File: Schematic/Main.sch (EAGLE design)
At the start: 83 parts, among them IC1 PIC18F4550_40, IC2 7805, IC4 AD7734, IC5 AD780, IC7 7805, K1 SRD-24VDC-SL-C, K2 SRD-24VDC-SL-C, Q1 20MHz, Q2 3.579545MHz, T1 2N2222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

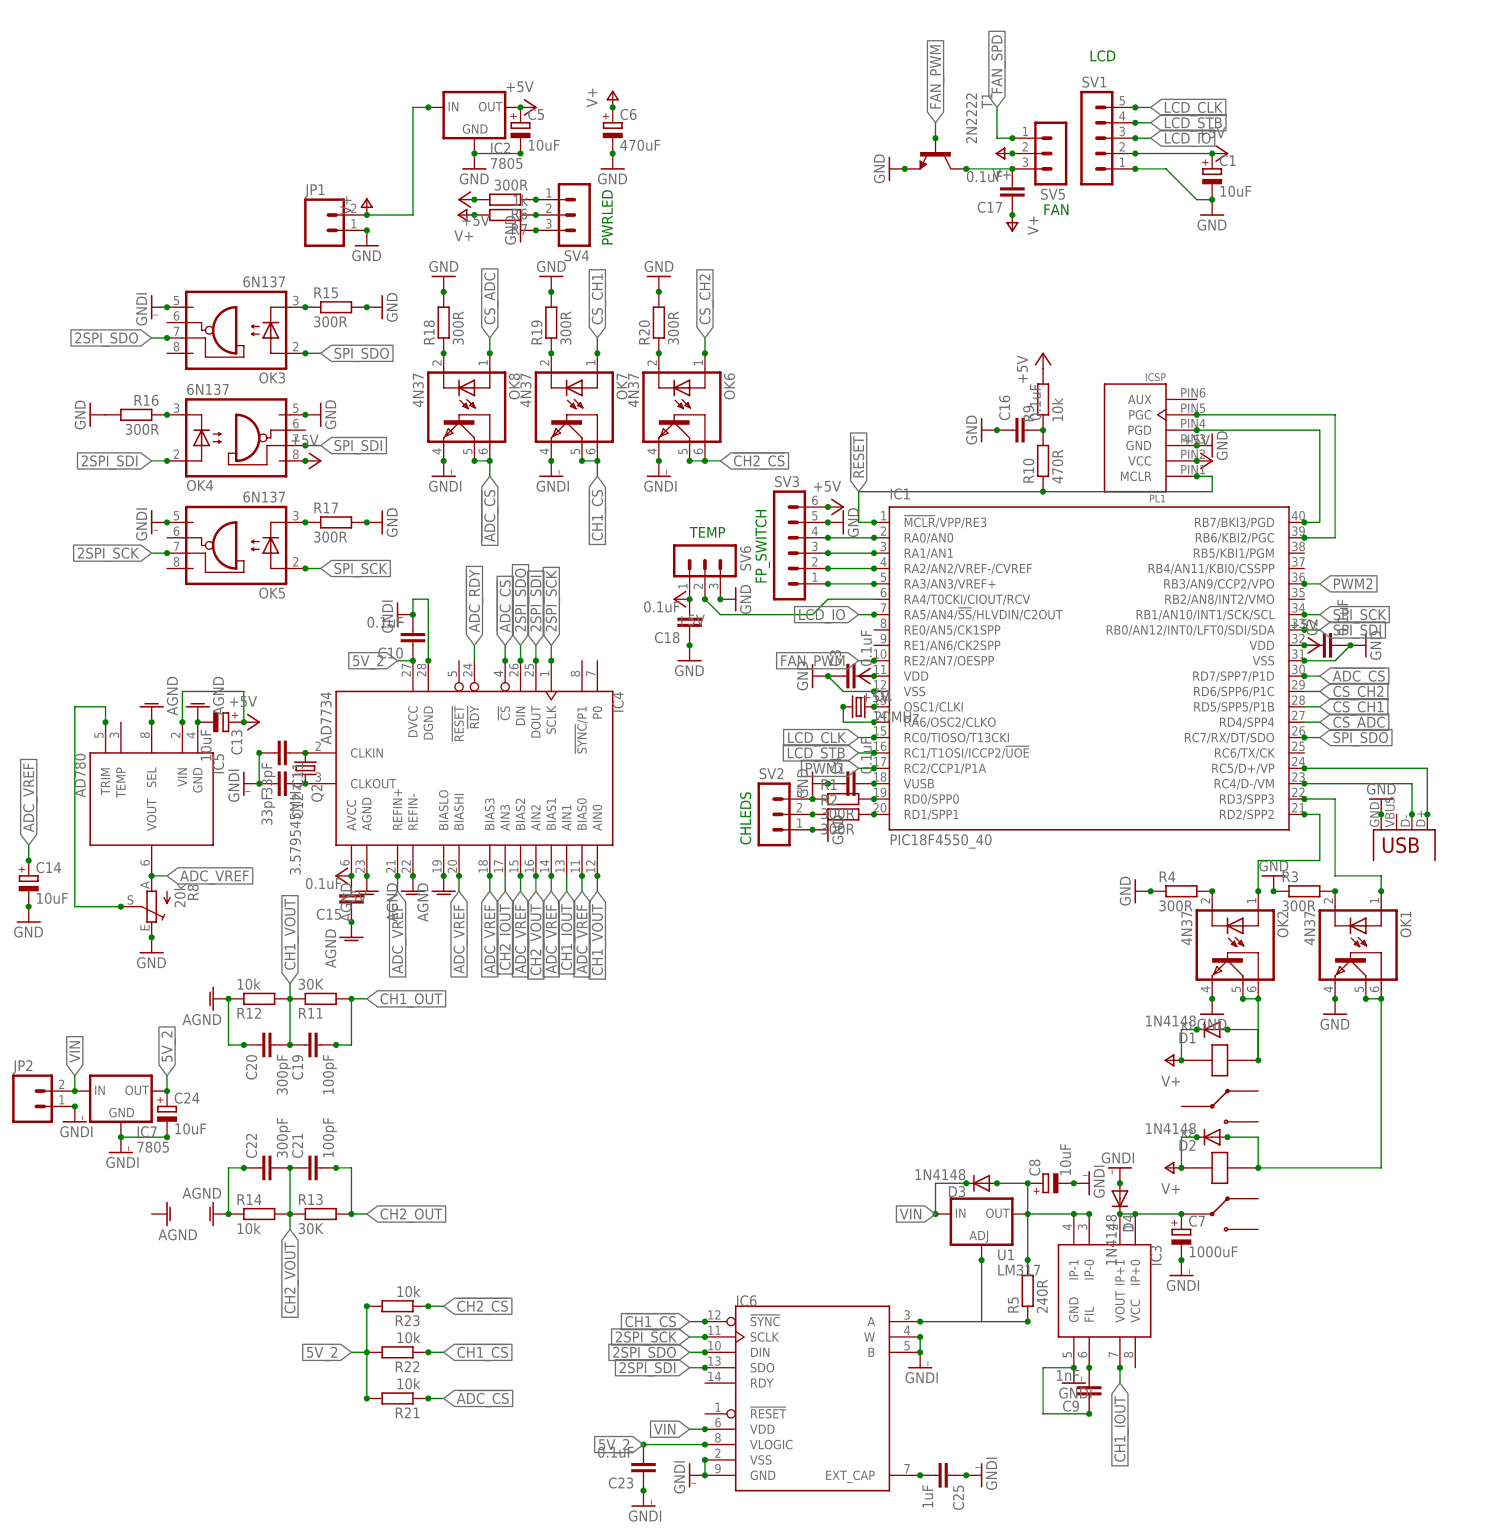
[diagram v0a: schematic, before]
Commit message: Got rid of the metric crapton of isolation as it wasn't really needed.
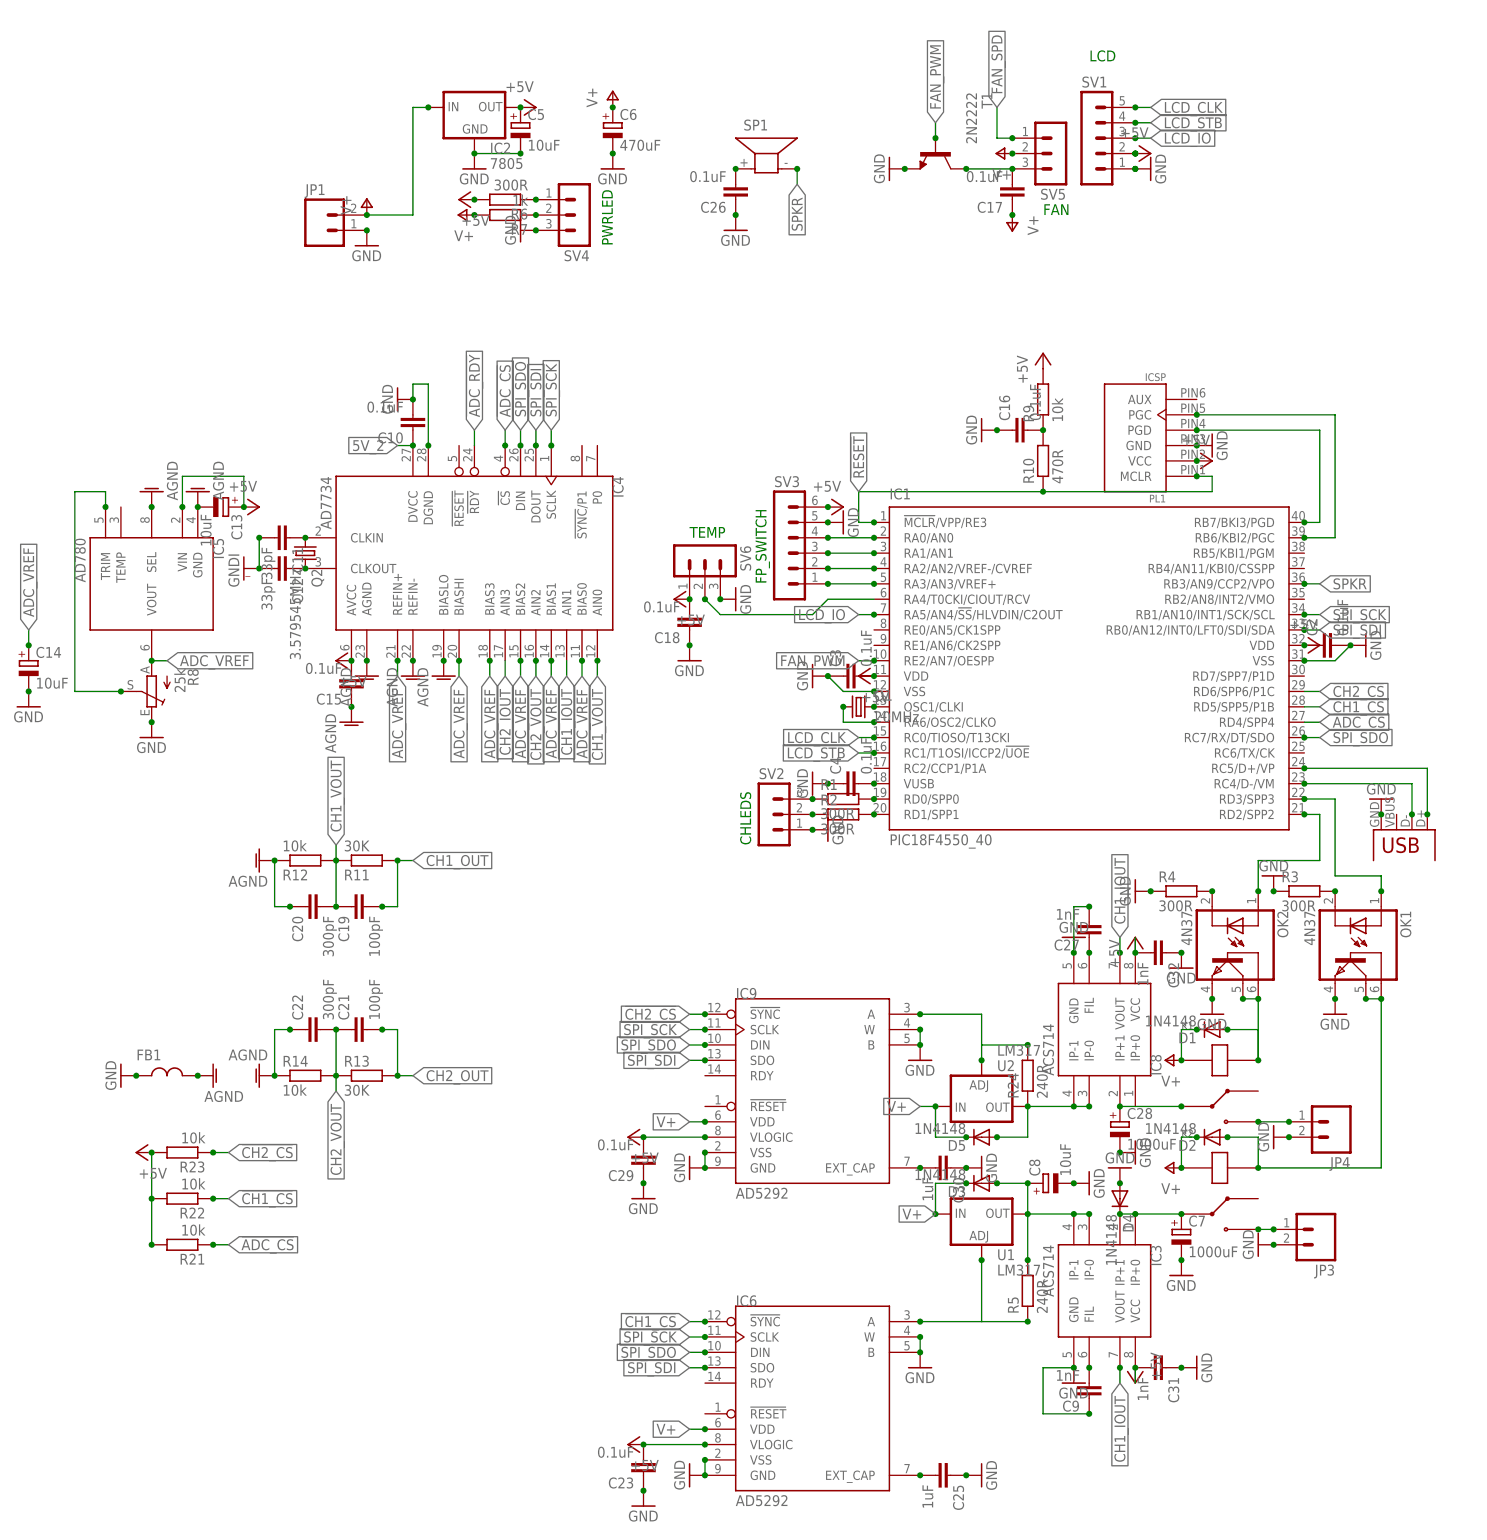
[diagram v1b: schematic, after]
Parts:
- removed C1, C24: 10uF, rcl:CPOL-EUE2.5-5
- removed IC7: 7805, v-reg:78MXXS
- removed JP2: (no value), SparkFun:M023.5MM
- removed OK3, OK4, OK5: 6N137, Particulates:6N137
- removed OK6, OK7, OK8: 4N37, optocoupler:4N37
- removed R15, R16, R17, R18, R19, R20: 300R, rcl:R-EU_0204/7
- added C26, C29: 0.1uF, rcl:C-EUC2012
- added C27, C31, C32: 1nF, rcl:C-EUC2012
- added C28: 1000uF, rcl:CPOL-EUE5-13
- added C30: 1uF, rcl:C-EUC2012
- added D5: 1N4148, diode:1N4148DO35-7
- added FB1: (no value), Particulates:FERRITE2012
- added IC8: ACS714, Particulates:ACS714SOIC8
- added IC9: AD5292, Particulates:AD5292TSSOP14
- added JP3, JP4: (no value), SparkFun:M023.5MM
- added R24: 240R, rcl:R-EU_0204/7
- added SP1: KSS1201, buzzer:KSS1201
- added U2: LM317, SparkFun:V_REG_317SINK
- C10, C11, C12, C15, C17, C18, C19, C2, C20, C21, C22, C23, C25, C3, C4, C9: device rcl:C-EU025-030X050 -> rcl:C-EUC2012
- IC3: value (none) -> ACS714
- IC6: value (none) -> AD5292
- R1, R10, R11, R12, R13, R14, R2, R21, R22, R23, R3, R4, R6, R7, R9: device rcl:R-EU_0204/7 -> rcl:R-EU_R2012
- R8: value 20k -> 25k
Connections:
- removed net 2SPI_SCK: IC4.SCLK, IC6.SCLK, OK5.VE
- removed net 2SPI_SDI: IC4.DOUT, IC6.SDO, OK4.A
- removed net 2SPI_SDO: IC4.DIN, IC6.DIN, OK3.VE
- removed net CS_ADC: IC1.RD4/SPP4, OK8.A
- removed net CS_CH1: IC1.RD5/SPP5/P1B, OK7.A
- removed net CS_CH2: IC1.RD6/SPP6/P1C, OK6.A
- removed net N$28: OK5.C, R17.1
- removed net N$34: OK4.C, R16.1
- removed net N$35: OK3.C, R15.1
- removed net N$36: OK8.C, R18.1
- removed net N$37: OK7.C, R19.1
- removed net N$38: OK6.C, R20.1
- removed net PWM1: IC1.RC2/CCP1/P1A
- removed net PWM2: IC1.RB3/AN9/CCP2/VPO
- removed net VIN: D3.C, IC6.VDD, IC7.IN, JP2.2, U1.IN
- new net N$23: C26.2, SP1.1
- new net N$41: JP4.1, K1.NO
- new net N$42: JP3.1, K2.NO
- new net N$43: C27.1, IC8.FIL
- new net N$44: D5.A, IC8.IP-0, IC8.IP-1, R24.1, U2.OUT
- new net N$46: C30.2, IC9.EXT_CAP
- new net N$47: IC9.A, R24.2, U2.ADJ
- new net SPKR: IC1.RB3/AN9/CCP2/VPO, SP1.2
- net !ADC_CS!: now also IC1.RD4/SPP4; no longer IC1.RD7/SPP7/P1D, OK8.BAS, OK8.COL
- net !CH1_CS!: now also IC1.RD5/SPP5/P1B; no longer OK7.BAS, OK7.COL
- net !CH2_CS!: now also IC1.RD6/SPP6/P1C, IC9.!SYNC!; no longer OK6.BAS, OK6.COL
- net +5V: now also C23.2, C29.2, C31.2, C32.2, IC3.VCC, IC6.VLOGIC, IC8.VCC, IC9.VLOGIC, R21.2, R22.2, R23.2; no longer C1.+, OK4.VCC
- net 5V_2: no longer C23.2, C24.+, IC6.VLOGIC, IC7.OUT, R21.2, R22.2, R23.2
- net AGND: now also FB1.P$2
- net CH1_IOUT: now also IC8.VOUT
- net CH2_OUT: now also C28.+, IC8.IP+0, IC8.IP+1, K1.IN
- net GND: now also C26.1, JP3.2, JP4.2; no longer C1.-, OK4.GND, R15.2, R16.2, R17.2, R18.2, R19.2, R20.2
- net GNDI: now also C27.2, C28.-, C29.1, C30.1, C31.1, C32.1, FB1.P$1, IC8.GND, IC9.B, IC9.GND, IC9.VSS, IC9.W; no longer C24.-, IC7.GND, JP2.1, OK3.GND, OK5.GND, OK6.EMI, OK7.EMI, OK8.EMI
- net SPI_SCK: now also IC4.SCLK, IC6.SCLK, IC9.SCLK; no longer OK5.A
- net SPI_SDI: now also IC4.DOUT, IC6.SDO, IC9.SDO; no longer OK4.VE
- net SPI_SDO: now also IC4.DIN, IC6.DIN, IC9.DIN; no longer OK3.A
- net V+: now also D3.C, D5.C, IC6.VDD, IC9.VDD, U1.IN, U2.IN
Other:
- moved on the sheet: C10, C11, C12, C13, C14, C15, C19, C20, C21, C22, IC4, IC5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

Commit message: Swapped PIC for AVR.
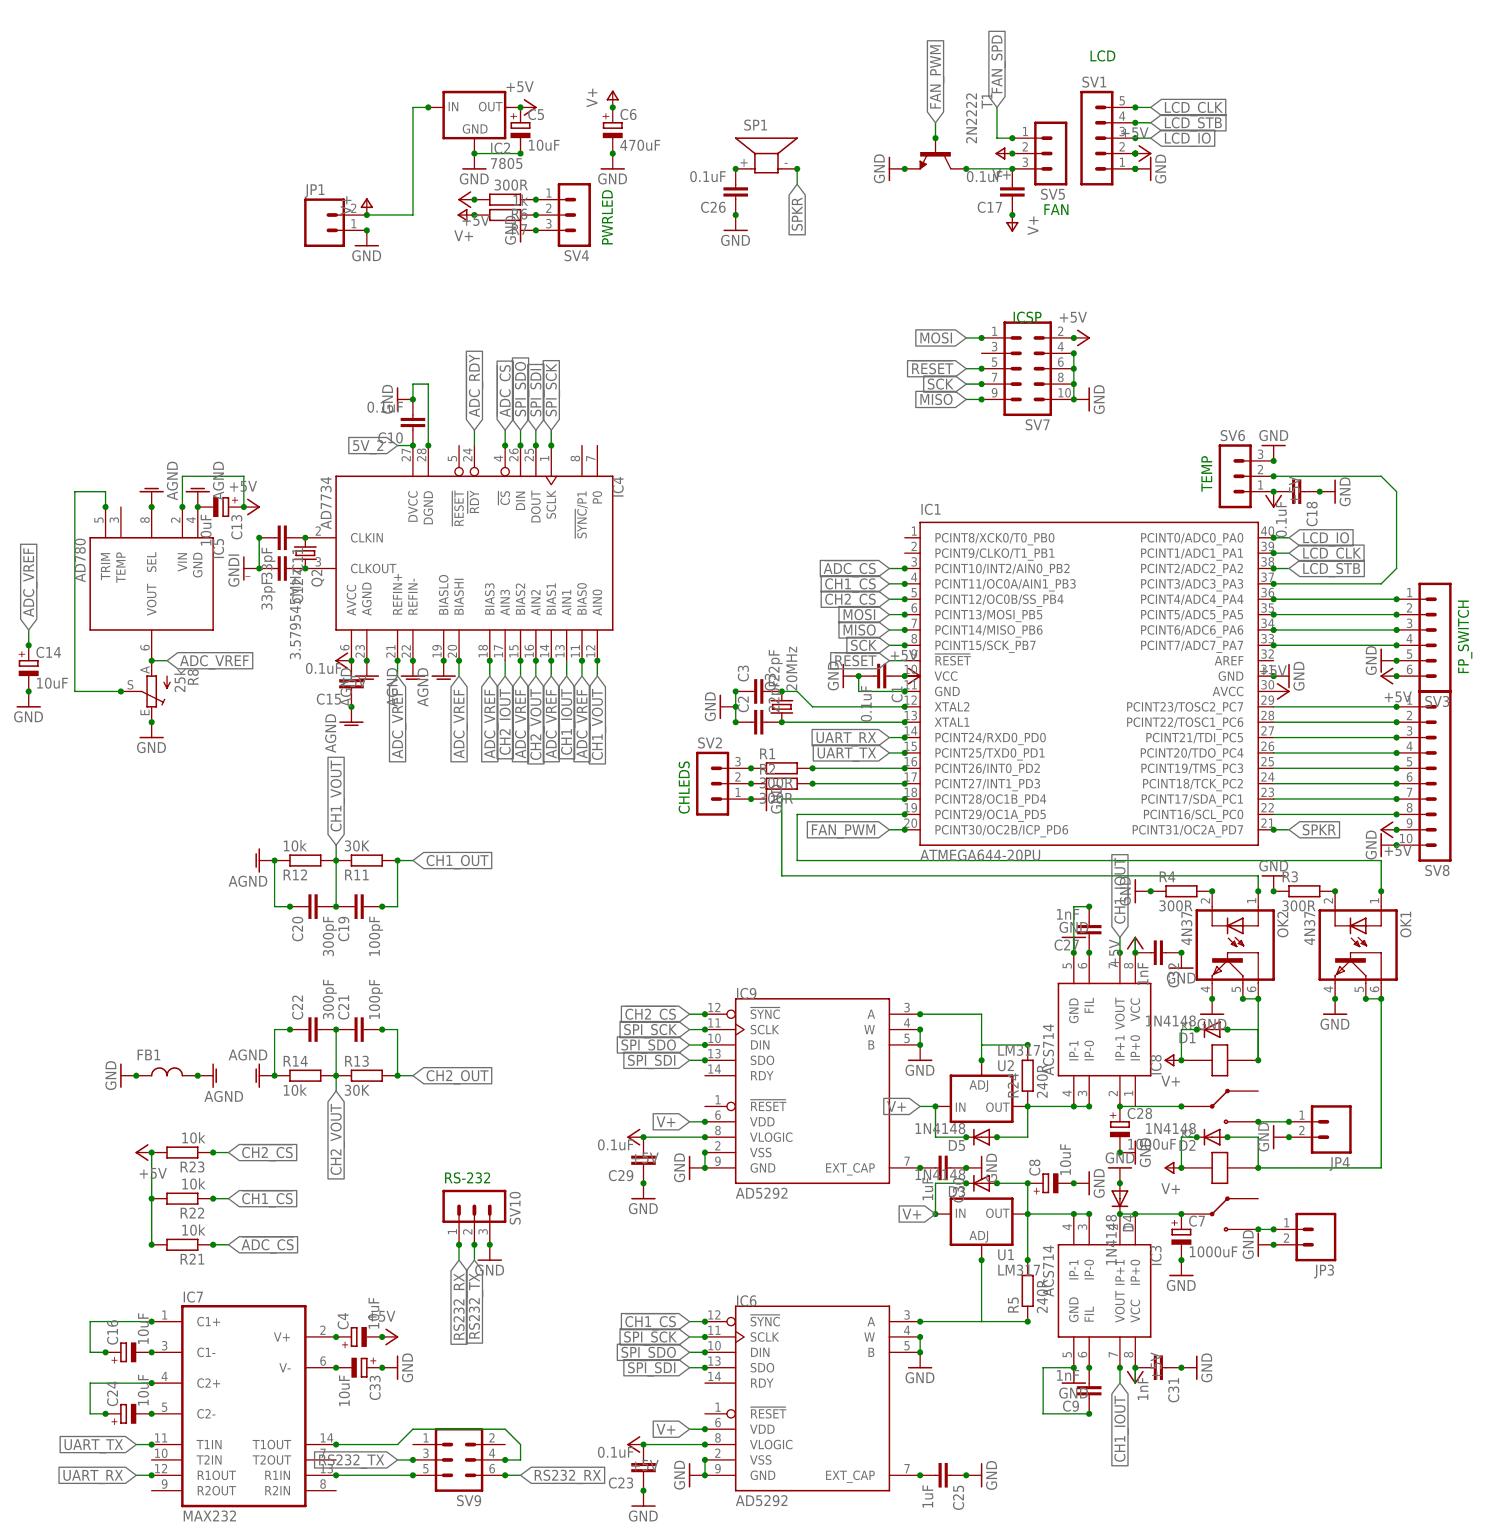
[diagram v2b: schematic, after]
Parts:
- removed PL1: ICSP, jason-test:ICSP
- removed Q1: 20MHz, crystal:CRYSTALHC49S
- removed R10: 470R, rcl:R-EU_R2012
- removed R9: 10k, rcl:R-EU_R2012
- removed X1: USBPTH, SparkFun:USBPTH
- added C1: 0.1uF, rcl:C-EUC2012
- added C24, C33: 10uF, rcl:CPOL-EUE2.5-5
- added IC7: MAX232, maxim:MAX232
- added Q3: 20MHz, crystal:CRYSTALHC49S
- added SV10: (no value), con-lstb:MA03-1
- added SV7: (no value), con-lstb:MA05-2
- added SV8: (no value), con-lstb:MA10-1
- added SV9: (no value), con-lstb:MA03-2
- C16: value 0.1uF -> 10uF; device rcl:C-EU025-030X050 -> rcl:CPOL-EUE2.5-5
- C2, C3: value 0.1uF -> 22pF; device rcl:C-EUC2012 -> rcl:C-EU025-024X044
- C4: value 0.1uF -> 10uF; device rcl:C-EUC2012 -> rcl:CPOL-EUE2.5-5
- IC1: value PIC18F4550_40 -> ATMEGA644-20PU; device microchip:PIC18F4550_40 -> atmel:ATMEGA644-20PU
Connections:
- new net MISO: IC1.PCINT14/MISO_PB6, SV7.9
- new net MOSI: IC1.PCINT13/MOSI_PB5, SV7.1
- new net N$28: IC1.PCINT18/TCK_PC2, SV8.6
- new net N$34: IC1.PCINT16/SCL_PC0, SV8.8
- new net N$35: IC7G$1.R1IN, SV9.5
- new net N$36: IC7G$1.T1OUT, SV9.4
- new net N$37: C24.-, IC7G$1.C2-
- new net N$38: C16.-, IC7G$1.C1-
- new net N$45: C24.+, IC7G$1.C2+
- new net N$48: C16.+, IC7G$1.C1+
- new net N$49: C33.-, IC7G$1.V-
- new net N$50: C4.+, IC7G$1.V+
- new net RS232_RX: SV10.1, SV9.6
- new net RS232_TX: SV10.2, SV9.3
- new net SCK: IC1.PCINT15/SCK_PB7, SV7.7
- new net UART_RX: IC1.PCINT24/RXD0_PD0, IC7G$1.R1OUT
- new net UART_TX: IC1.PCINT25/TXD0_PD1, IC7G$1.T1IN
- net !ADC_CS!: now also IC1.PCINT10/INT2/AIN0_PB2; no longer IC1.RD4/SPP4
- net !CH1_CS!: now also IC1.PCINT11/OC0A/AIN1_PB3; no longer IC1.RD5/SPP5/P1B
- net !CH2_CS!: now also IC1.PCINT12/OC0B/SS_PB4; no longer IC1.RD6/SPP6/P1C
- net !LCD_STB!: now also IC1.PCINT2/ADC2_PA2; no longer IC1.RC1/T1OSI/ICCP2/!UOE
- net !RESET!: now also IC1.!RESET, SV7.5; no longer IC1.!MCLR!/VPP/RE3, PL1.MCLR, R10.1
- net +5V: now also C1.1, C4.-, IC1.AVCC, IC1.VCC, SV7.2, SV8.9; no longer C2.1, C3.2, IC1.VDD, IC1.VDD@1, PL1.VCC, R9.2
- net FAN_PWM: now also IC1.PCINT30/OC2B/ICP_PD6; no longer IC1.RE2/AN7/OESPP
- net GND: now also C1.2, C2.1, C33.+, IC1.GND, IC1.GND@1, SV10.3, SV7.10, SV7.4, SV7.6, SV7.8, SV8.10; no longer C16.1, C2.2, C4.1, IC1.VSS, IC1.VSS@1, PL1.GND, X1.GND
- net LCD_CLK: now also IC1.PCINT1/ADC1_PA1; no longer IC1.RC0/TIOSO/T13CKI
- net LCD_IO: now also IC1.PCINT0/ADC0_PA0; no longer IC1.RA5/AN4/!SS!/HLVDIN/C2OUT
- net N$1: now also C3.2, IC1.XTAL2, Q3.2; no longer C4.2, IC1.VUSB
- net N$10: now also IC1.PCINT6/ADC6_PA6; no longer IC1.RA1/AN1
- net N$11: now also IC1.PCINT7/ADC7_PA7; no longer IC1.RA0/AN0
- net N$12: now also IC1.PCINT4/ADC4_PA4; no longer IC1.RA3/AN3/VREF+
- net N$13: now also IC1.PCINT26/INT0_PD2, R1.2; no longer IC1.OSC1/CLKI, Q1.2
- net N$14: now also IC1.PCINT23/TOSC2_PC7, SV8.1; no longer IC1.RA6/OSC2/CLKO, Q1.1
- net N$15: now also IC1.PCINT22/TOSC1_PC6, SV8.2; no longer IC1.RC4/D-/VM, X1.D-
- net N$16: now also IC1.PCINT21/TDI_PC5, SV8.3; no longer IC1.RC5/D+/VP, X1.D+
- net N$19: now also IC1.PCINT20/TDO_PC4, SV8.4; no longer IC1.RD2/SPP2, OK2.A
- net N$2: now also C2.2, IC1.XTAL1, Q3.1; no longer C16.2, R10.2, R9.1
- net N$20: now also IC1.PCINT19/TMS_PC3, SV8.5; no longer IC1.RD3/SPP3, OK1.A
- net N$3: now also IC1.PCINT28/OC1B_PD4, OK2.A; no longer IC1.RB6/KBI2/PGC, PL1.PGC
- net N$30: now also IC1.PCINT17/SDA_PC1, SV8.7; no longer IC1.RA4/T0CKI/CIOUT/RCV, SV6.2
- net N$4: now also IC1.PCINT29/OC1A_PD5, OK1.A; no longer IC1.RB7/BKI3/PGD, PL1.PGD
- net N$5: now also IC1.PCINT3/ADC3_PA3, SV6.2; no longer IC1.RD0/SPP0, R1.2
- net N$6: now also IC1.PCINT27/INT1_PD3; no longer IC1.RD1/SPP1
- net N$9: now also IC1.PCINT5/ADC5_PA5; no longer IC1.RA2/AN2/VREF-/CVREF
- net SPI_SCK: no longer IC1.RB1/AN10/INT1/SCK/SCL
- net SPI_SDI: no longer IC1.RB0/AN12/INT0/LFT0/SDI/SDA
- net SPI_SDO: no longer IC1.RC7/RX/DT/SDO
- net SPKR: now also IC1.PCINT31/OC2A_PD7; no longer IC1.RB3/AN9/CCP2/VPO
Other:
- note added: "ICSP"
- note added: "RS-232"
- moved on the sheet: C18, C2, C3, IC1, R1, R2, SV2, SV3, SV6
